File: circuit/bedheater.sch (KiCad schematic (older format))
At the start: 20 parts, among them CON1 AVR-ISP-6, CON2 BARREL_JACK, IC1 ATMEGA328-P, P1 Heater+, P2 CONN_01X02, P3 Heater-, Q1 TIP142, U1 OKI-78SR-3.3, U2 UB232R, Y1 20 MHz

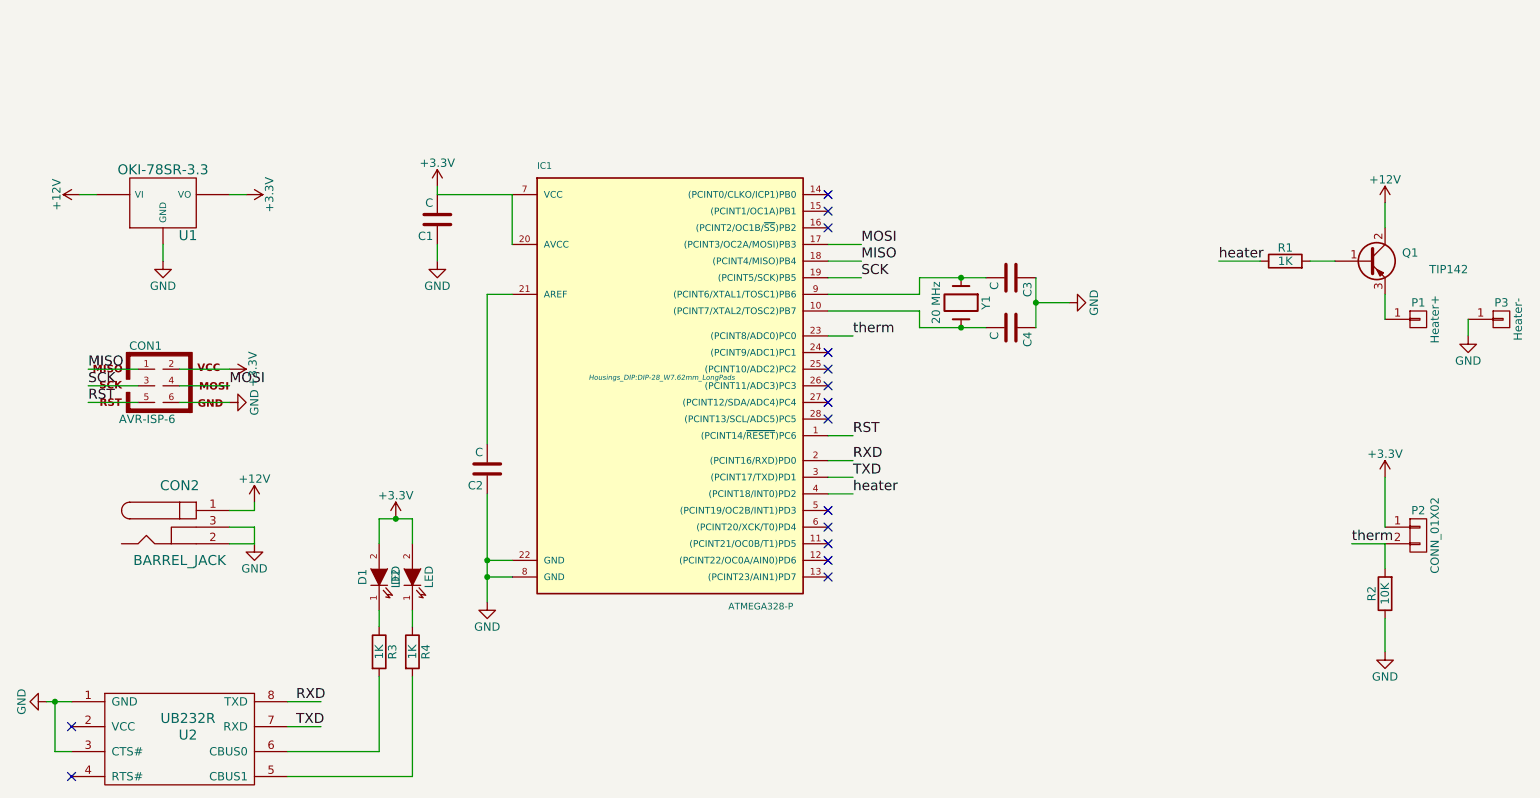
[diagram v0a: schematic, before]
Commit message: Update PID params. Fix schematic/pcb issue where the TIP142 was connected as though it were PNP (it is an NPN BJT). Correct some connectivity issues in the app
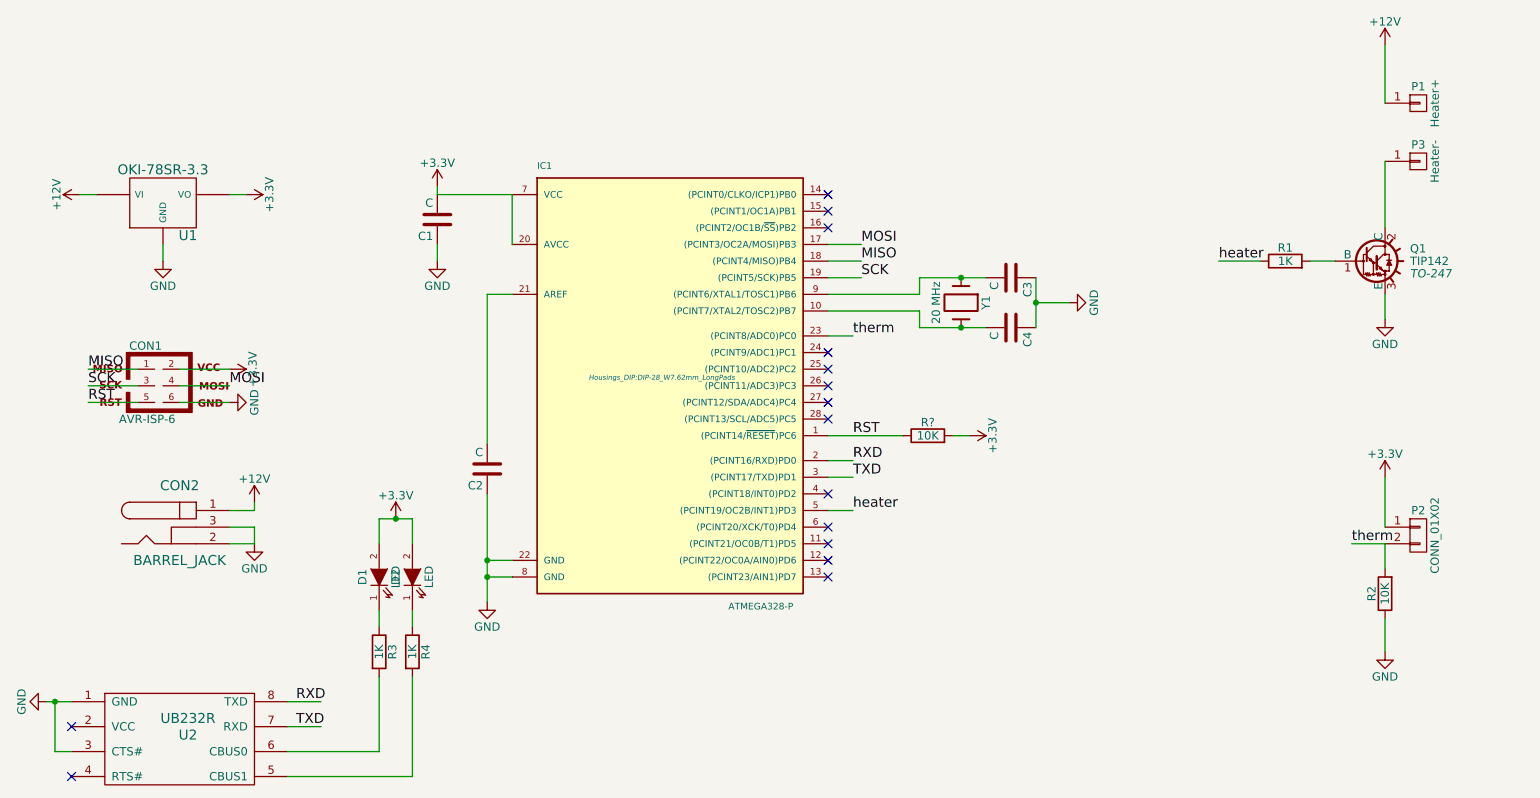
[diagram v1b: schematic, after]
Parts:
- removed Q1: TIP142, TO_SOT_Packages_THT:TO-247_Horizontal_Neutral123_largePads, symbol Q_PNP_BCE
- added Q1: TIP142, TO-247, symbol TIP120
- added R?: 10K, Resistors_ThroughHole:Resistor_Horizontal_RM10mm, symbol R
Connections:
- net +12V: now also P1.1 (P1)
- net +3V3: now also R?.2
- net GND: now also Q1.3 (E); no longer P3.1 (P1)
- net RST: now also R?.1
- net heater: now also IC1.5 ((PCINT19/OC2B/INT1)PD3); no longer IC1.4 ((PCINT18/INT0)PD2)
- net at R1.2: now also Q1.1 (B)
- new net: P3.1 (P1), Q1.2 (C)
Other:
- moved on the sheet: P1, P3
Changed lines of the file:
@@
-$EndComp
-$Comp
-L Q_PNP_BCE Q1
-U 1 1 56AF000F
-P 9550 2650
-F 0 "Q1" H 9850 2700 50  0000 R CNN
-F 1 "TIP142" H 10150 2600 50  0000 R CNN
-F 2 "TO_SOT_Packages_THT:TO-247_Horizontal_Neutral123_largePads" H 9750 2750 29  0001 C CNN
-F 3 "" H 9550 2650 60  0000 C CNN
-	1    9550 2650
-	1    0    0    -1
 $EndComp
 $Comp
@@
 therm
 $Comp
-L GND #PWR18
-U 1 1 56AF05EC
-P 10150 3100
-F 0 "#PWR18" H 10150 2850 50  0001 C CNN
-F 1 "GND" H 10150 2950 50  0000 C CNN
-F 2 "" H 10150 3100 60  0000 C CNN
-F 3 "" H 10150 3100 60  0000 C CNN
-	1    10150 3100
-	1    0    0    -1
-$EndComp
-$Comp
-L +12V #PWR15
+L +12V #PWR14
 U 1 1 56AF0632
-P 9650 2300
-F 0 "#PWR15" H 9650 2150 50  0001 C CNN
-F 1 "+12V" H 9650 2440 50  0000 C CNN
-F 2 "" H 9650 2300 60  0000 C CNN
-F 3 "" H 9650 2300 60  0000 C CNN
-	1    9650 2300
+P 9650 1350
+F 0 "#PWR14" H 9650 1200 50  0001 C CNN
+F 1 "+12V" H 9650 1490 50  0000 C CNN
+F 2 "" H 9650 1350 60  0000 C CNN
+F 3 "" H 9650 1350 60  0000 C CNN
+	1    9650 1350
 	1    0    0    -1
 $EndComp
@@
 $EndComp
 $Comp
-L +3.3V #PWR11
+L +3.3V #PWR10
 U 1 1 56AF0784
 P 3950 2200
-F 0 "#PWR11" H 3950 2050 50  0001 C CNN
+F 0 "#PWR10" H 3950 2050 50  0001 C CNN
 F 1 "+3.3V" H 3950 2340 50  0000 C CNN
 F 2 "" H 3950 2200 60  0000 C CNN
@@
 $EndComp
 $Comp
-L GND #PWR13
+L GND #PWR12
 U 1 1 56AF07D9
 P 4250 4700
-F 0 "#PWR13" H 4250 4450 50  0001 C CNN
+F 0 "#PWR12" H 4250 4450 50  0001 C CNN
 F 1 "GND" H 4250 4550 50  0000 C CNN
 F 2 "" H 4250 4700 60  0000 C CNN
@@
 $EndComp
 $Comp
-L GND #PWR12
+L GND #PWR11
 U 1 1 56AF09D6
 P 3950 2650
-F 0 "#PWR12" H 3950 2400 50  0001 C CNN
+F 0 "#PWR11" H 3950 2400 50  0001 C CNN
 F 1 "GND" H 3950 2500 50  0000 C CNN
 F 2 "" H 3950 2650 60  0000 C CNN
@@
 Text Label 8650 2650 0    60   ~ 0
 heater
-Text Label 6450 4050 0    60   ~ 0
+Text Label 6450 4150 0    60   ~ 0
 heater
 $Comp
-L GND #PWR14
+L GND #PWR13
 U 1 1 56AF0D03
 P 7750 2900
-F 0 "#PWR14" H 7750 2650 50  0001 C CNN
+F 0 "#PWR13" H 7750 2650 50  0001 C CNN
 F 1 "GND" H 7750 2750 50  0000 C CNN
 F 2 "" H 7750 2900 60  0000 C CNN
@@
 NoConn ~ 6300 3500
 NoConn ~ 6300 3600
-NoConn ~ 6300 4150
+NoConn ~ 6300 4050
 NoConn ~ 6300 4250
 NoConn ~ 6300 4350
@@
 L CONN_01X01 P1
 U 1 1 56EDC046
-P 9850 3000
-F 0 "P1" H 9850 3100 50  0000 C CNN
-F 1 "Heater+" V 9950 3000 50  0000 C CNN
-F 2 "Connect:Banana_Jack_1Pin" H 9850 3000 60  0001 C CNN
-F 3 "" H 9850 3000 60  0000 C CNN
-	1    9850 3000
+P 9850 1700
+F 0 "P1" H 9850 1800 50  0000 C CNN
+F 1 "Heater+" V 9950 1700 50  0000 C CNN
+F 2 "Connect:Banana_Jack_1Pin" H 9850 1700 60  0001 C CNN
+F 3 "" H 9850 1700 60  0000 C CNN
+	1    9850 1700
 	1    0    0    -1
 $EndComp
@@
 L CONN_01X01 P3
 U 1 1 56EDC11B
-P 10350 3000
-F 0 "P3" H 10350 3100 50  0000 C CNN
-F 1 "Heater-" V 10450 3000 50  0000 C CNN
-F 2 "Connect:Banana_Jack_1Pin" H 10350 3000 60  0001 C CNN
-F 3 "" H 10350 3000 60  0000 C CNN
-	1    10350 3000
+P 9850 2050
+F 0 "P3" H 9850 2150 50  0000 C CNN
+F 1 "Heater-" V 9950 2050 50  0000 C CNN
+F 2 "Connect:Banana_Jack_1Pin" H 9850 2050 60  0001 C CNN
+F 3 "" H 9850 2050 60  0000 C CNN
+	1    9850 2050
 	1    0    0    -1
 $EndComp
@@
 TXD
 $Comp
-L +3.3V #PWR?
+L +3.3V #PWR9
 U 1 1 56F2FA59
 P 3700 4200
-F 0 "#PWR?" H 3700 4050 50  0001 C CNN
+F 0 "#PWR9" H 3700 4050 50  0001 C CNN
 F 1 "+3.3V" H 3700 4340 50  0000 C CNN
 F 2 "" H 3700 4200 60  0000 C CNN
@@
 	6300 3100 6450 3100
 Wire Wire Line
-	10150 3100 10150 3000
-Wire Wire Line
-	9650 3000 9650 2850
-Wire Wire Line
-	9650 2450 9650 2300
-Wire Wire Line
 	3950 2200 3950 2250
 Wire Wire Line
@@
 	8900 2650 8650 2650
 Wire Wire Line
-	6300 4050 6450 4050
+	6300 4150 6450 4150
 Wire Wire Line
 	6300 2850 6850 2850
@@
 	6300 2750 6500 2750
 Wire Wire Line
-	6300 3700 6450 3700
+	6300 3700 6750 3700
 Wire Wire Line
 	1900 2250 1800 2250
@@
 	2850 4350 2700 4350
 Wire Wire Line
-	1750 5300 1600 5300
+	1600 5300 1750 5300
 Wire Wire Line
 	3050 5300 3250 5300
@@
 	1650 5600 1650 5300
 Connection ~ 1650 5300
+$Comp
+L TIP120 Q1
+U 1 1 56F34CF0
+P 9550 2650
+F 0 "Q1" H 9800 2725 50  0000 L CNN
+F 1 "TIP142" H 9800 2650 50  0000 L CNN
+F 2 "TO-247" H 9800 2575 50  0000 L CIN
+F 3 "" H 9550 2650 50  0000 L CNN
+	1    9550 2650
+	1    0    0    -1
+$EndComp
+Wire Wire Line
+	9650 1700 9650 1350
+Wire Wire Line
+	9650 2050 9650 2450
+$Comp
+L GND #PWR15
+U 1 1 56F34F79
+P 9650 3000
+F 0 "#PWR15" H 9650 2750 50  0001 C CNN
+F 1 "GND" H 9650 2850 50  0000 C CNN
+F 2 "" H 9650 3000 60  0000 C CNN
+F 3 "" H 9650 3000 60  0000 C CNN
+	1    9650 3000
+	1    0    0    -1
+$EndComp
+Wire Wire Line
+	9650 2850 9650 3000
+$Comp
+L R R?
+U 1 1 56F35230
+P 6900 3700
+F 0 "R?" V 6980 3700 50  0000 C CNN
+F 1 "10K" V 6900 3700 50  0000 C CNN
+F 2 "Resistors_ThroughHole:Resistor_Horizontal_RM10mm" V 6830 3700 30  0001 C CNN
+F 3 "" H 6900 3700 30  0000 C CNN
+	1    6900 3700
+	0    -1   -1   0
+$EndComp
+$Comp
+L +3.3V #PWR?
+U 1 1 56F353E1
+P 7150 3700
+F 0 "#PWR?" H 7150 3550 50  0001 C CNN
+F 1 "+3.3V" H 7150 3840 50  0000 C CNN
+F 2 "" H 7150 3700 60  0000 C CNN
+F 3 "" H 7150 3700 60  0000 C CNN
+	1    7150 3700
+	0    1    1    0
+$EndComp
+Wire Wire Line
+	7150 3700 7050 3700
 $EndSCHEMATC
